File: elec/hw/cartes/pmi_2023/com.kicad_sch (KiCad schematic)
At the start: 37 parts, among them J7 USB4105-GF-A-060, Q2 2N7002, SW10 TS-1187A-B-A-B, SW7 MSS12C02LS-BB2.0, U32 ESP32-S3-WROOM-1

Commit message: small changes
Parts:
- SW10: footprint cocotter_others:TS-1187A-B-A-B -> cocotter_others:TSB001A3526A02; symbol cocotter_others:TS-1187A-B-A-B -> cocotter_others:TSB001A3526A02; JLCPCB C318884 -> C2888889
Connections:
- net EN_ESP32_3v3: now also SW10.2; no longer SW10.B (2)
- net GND_m: now also SW10.1; no longer SW10.A (1)
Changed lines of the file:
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@@
 	)
 	(symbol
-		(lib_id "cocotter_others:TS-1187A-B-A-B")
+		(lib_id "cocotter_others:TSB001A3526A02")
 		(at 69.85 148.59 90)
 		(unit 1)
@@
 			)
 		)
-		(property "Footprint" "cocotter_others:TS-1187A-B-A-B"
+		(property "Footprint" "cocotter_others:TSB001A3526A02"
 			(at 69.85 148.59 0)
 			(effects
@@
 			)
 		)
-		(property "Datasheet" ""
+		(property "Datasheet" "https://wmsc.lcsc.com/wmsc/upload/file/pdf/v2/lcsc/2108252230_BZCN-TSB001A3526A02_C2888889.pdf"
 			(at 74.93 148.59 0)
 			(effects
@@
 			)
 		)
-		(property "JLCPCB" "C318884"
+		(property "JLCPCB" "C2888889"
 			(at 74.93 149.86 0)
 			(effects
@@
 			)
 		)
-		(pin "A"
+		(pin "1"
 		)
-		(pin "B"
+		(pin "2"
 		)
 		(instances

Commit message: PAMI 2023: update jlc part number
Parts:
- R100, R82, R83, R91, R92, R97, R98, R99: JLCPCB C2991540 -> C21190
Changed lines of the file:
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@@
 			)
 		)
-		(property "JLCPCB" "C2991540"
+		(property "JLCPCB" "C21190"
 			(at 69.85 87.63 0)
 			(effects
@@
 			)
 		)
-		(property "JLCPCB" "C2991540"
+		(property "JLCPCB" "C21190"
 			(at 29.21 177.8 0)
 			(effects
@@
 			)
 		)
-		(property "JLCPCB" "C2991540"
+		(property "JLCPCB" "C21190"
 			(at 220.98 92.71 0)
 			(effects
@@
 			)
 		)
-		(property "JLCPCB" "C2991540"
+		(property "JLCPCB" "C21190"
 			(at 39.37 177.8 0)
 			(effects
@@
 			)
 		)
-		(property "JLCPCB" "C2991540"
+		(property "JLCPCB" "C21190"
 			(at 220.98 101.6 0)
 			(effects
@@
 			)
 		)
-		(property "JLCPCB" "C2991540"
+		(property "JLCPCB" "C21190"
 			(at 58.42 87.63 0)
 			(effects
@@
 			)
 		)
-		(property "JLCPCB" "C2991540"
+		(property "JLCPCB" "C21190"
 			(at 58.42 77.47 0)
 			(effects
@@
 			)
 		)
-		(property "JLCPCB" "C2991540"
+		(property "JLCPCB" "C21190"
 			(at 69.85 77.47 0)
 			(effects

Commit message: encoder resistors values corrected
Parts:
- SW10: value TS-1187A-B-A-B -> TSB001A3526A02
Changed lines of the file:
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@@
 			)
 		)
-		(property "Value" "TS-1187A-B-A-B"
+		(property "Value" "TSB001A3526A02"
 			(at 74.93 146.05 0)
 			(effects

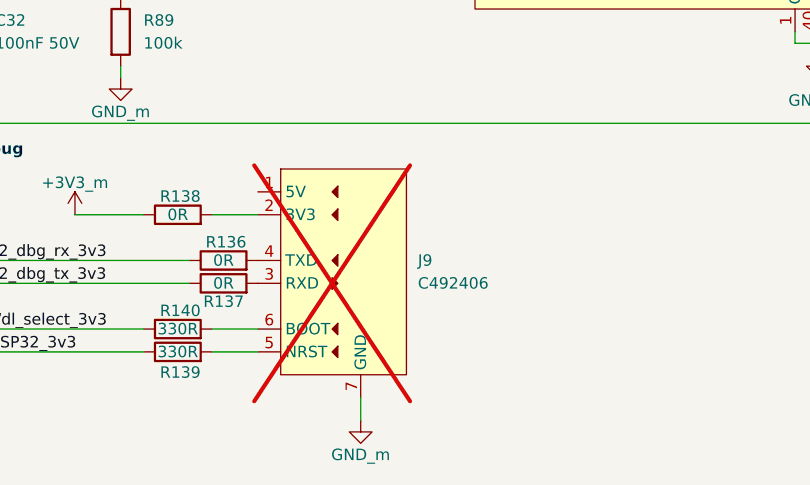
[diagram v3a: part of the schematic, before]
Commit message: XRA1200 replaced by TCA6408
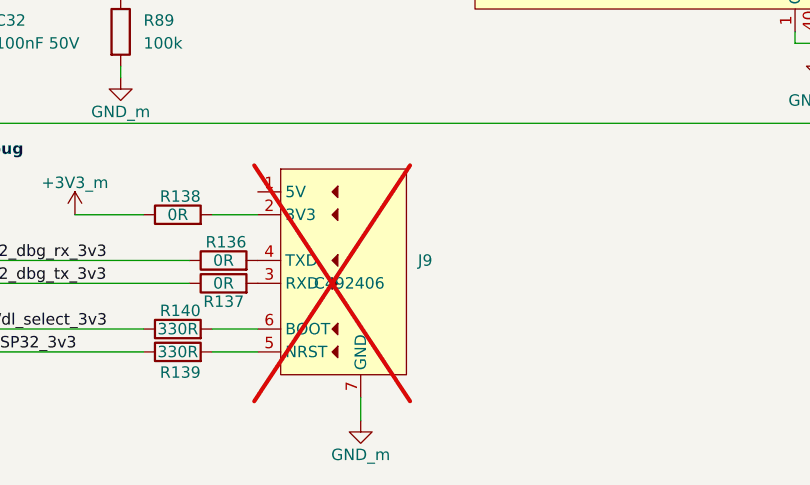
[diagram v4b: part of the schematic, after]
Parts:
- C32, C33, C34: JLCPCB C14663 -> (none); JLCPCB Part # (none) -> C14663
- C35: JLCPCB C15850 -> (none); JLCPCB Part # (none) -> C15850
- D4, D5: JLCPCB C2290 -> (none); JLCPCB Part # (none) -> C2290
- J7: JLCPCB C2927039 -> (none); JLCPCB Part # (none) -> C2927039
- J9: JLCPCB C492406 -> (none); JLCPCB Part # (none) -> C492406
- Q2: JLCPCB C8545 -> (none); JLCPCB Part # (none) -> C8545
- R100, R82, R83, R91, R92, R97, R98, R99: JLCPCB C21190 -> (none); JLCPCB Part # (none) -> C2991540
- R136, R137, R138: JLCPCB C431718 -> (none); JLCPCB Part # (none) -> C431718
- R139, R140: JLCPCB C23138 -> (none); JLCPCB Part # (none) -> C23138
- R84, R85, R86, R88, R89, R90, R93, R95, R96: JLCPCB C25803 -> (none); JLCPCB Part # (none) -> C25803
- R87: JLCPCB C23265 -> (none); JLCPCB Part # (none) -> C23265
- R94: JLCPCB C25804 -> (none); JLCPCB Part # (none) -> C25804
- SW10: JLCPCB C2888889 -> (none); JLCPCB Part # (none) -> C2888889
- SW7: JLCPCB C3008585 -> (none); JLCPCB Part # (none) -> C3008585
- U32: JLCPCB C2913204 -> (none); JLCPCB Part # (none) -> C2913204
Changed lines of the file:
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@@
 			)
 		)
-		(property "JLCPCB" "C25803"
+		(property "JLCPCB Part #" "C25803"
 			(at 97.79 130.81 0)
 			(effects
@@
 			)
 		)
-		(property "JLCPCB" "C15850"
+		(property "JLCPCB Part #" "C15850"
 			(at 208.28 33.02 0)
 			(effects
@@
 			)
 		)
-		(property "JLCPCB" "C23138"
+		(property "JLCPCB Part #" "C23138"
 			(at 104.14 181.61 0)
 			(effects
@@
 			)
 		)
-		(property "JLCPCB" "C2888889"
+		(property "JLCPCB Part #" "C2888889"
 			(at 74.93 149.86 0)
 			(effects
@@
 			)
 		)
-		(property "JLCPCB" "C8545"
+		(property "JLCPCB Part #" "C8545"
 			(at 234.95 144.78 0)
 			(effects
@@
 			)
 		)
-		(property "JLCPCB" "C14663"
+		(property "JLCPCB Part #" "C14663"
 			(at 186.69 33.02 0)
 			(effects
@@
 			)
 		)
-		(property "JLCPCB" "C25803"
+		(property "JLCPCB Part #" "C25803"
 			(at 85.09 63.5 0)
 			(effects
@@
 			)
 		)
-		(property "JLCPCB" "C2290"
+		(property "JLCPCB Part #" "C2290"
 			(at 29.21 185.42 0)
 			(effects
@@
 			)
 		)
-		(property "JLCPCB" "C25804"
+		(property "JLCPCB Part #" "C25804"
 			(at 229.87 125.73 0)
 			(effects
@@
 			)
 		)
-		(property "JLCPCB" "C25803"
+		(property "JLCPCB Part #" "C25803"
 			(at 82.55 130.81 0)
 			(effects
@@
 			)
 		)
-		(property "JLCPCB" "C23138"
+		(property "JLCPCB Part #" "C23138"
 			(at 104.14 184.15 0)
 			(effects
@@
 			)
 		)
-		(property "JLCPCB" "C14663"
+		(property "JLCPCB Part #" "C14663"
 			(at 93.98 60.96 0)
 			(effects
@@
 			)
 		)
-		(property "JLCPCB" "C14663"
+		(property "JLCPCB Part #" "C14663"
 			(at 80.01 148.59 0)
 			(effects
@@
 			)
 		)
-		(property "JLCPCB" "C431718"
+		(property "JLCPCB Part #" "C431718"
 			(at 109.22 176.53 0)
 			(effects
@@
 			)
 		)
-		(property "JLCPCB" "C2290"
+		(property "JLCPCB Part #" "C2290"
 			(at 39.37 185.42 0)
 			(effects
@@
 			)
 		)
-		(property "JLCPCB" "C21190"
+		(property "JLCPCB Part #" "C2991540"
 			(at 69.85 87.63 0)
 			(effects
@@
 			)
 		)
-		(property "JLCPCB" "C3008585"
+		(property "JLCPCB Part #" "C3008585"
 			(at 227.33 133.35 0)
 			(effects
@@
 			)
 		)
-		(property "JLCPCB" "C21190"
+		(property "JLCPCB Part #" "C2991540"
 			(at 29.21 177.8 0)
 			(effects
@@
 			)
 		)
-		(property "JLCPCB" "C21190"
+		(property "JLCPCB Part #" "C2991540"
 			(at 220.98 92.71 0)
 			(effects
@@
 			)
 		)
-		(property "JLCPCB" "C25803"
+		(property "JLCPCB Part #" "C25803"
 			(at 243.84 146.05 0)
 			(effects
@@
 			)
 		)
-		(property "JLCPCB" "C23265"
+		(property "JLCPCB Part #" "C23265"
 			(at 93.98 50.8 0)
 			(effects
@@
 			)
 		)
-		(property "JLCPCB" "C21190"
+		(property "JLCPCB Part #" "C2991540"
 			(at 39.37 177.8 0)
 			(effects
@@
 			)
 		)
-		(property "JLCPCB" "C25803"
+		(property "JLCPCB Part #" "C25803"
 			(at 85.09 50.8 0)
 			(effects
@@
 			)
 		)
-		(property "JLCPCB" "C431718"
+		(property "JLCPCB Part #" "C431718"
 			(at 104.14 168.91 0)
 			(effects
@@
 			)
 		)
-		(property "JLCPCB" "C21190"
+		(property "JLCPCB Part #" "C2991540"
 			(at 220.98 101.6 0)
 			(effects
@@
 			)
 		)
-		(property "JLCPCB" "C492406"
-			(at 130.81 176.5299 0)
+		(property "JLCPCB Part #" "C492406"
+			(at 123.19 176.53 0)
 			(effects
 				(font
 					(size 1.27 1.27)
 				)
-				(justify left)
 			)
 		)
@@
 			)
 		)
-		(property "JLCPCB" "C25803"
+		(property "JLCPCB Part #" "C25803"
 			(at 217.17 135.89 0)
 			(effects
@@
 			)
 		)
-		(property "JLCPCB" "C2927039"
+		(property "JLCPCB Part #" "C2927039"
 			(at 273.05 109.22 0)
 			(effects
@@
 			)
 		)
-		(property "JLCPCB" "C21190"
+		(property "JLCPCB Part #" "C2991540"
 			(at 58.42 87.63 0)
 			(effects
@@
 			)
 		)
-		(property "JLCPCB" "C21190"
+		(property "JLCPCB Part #" "C2991540"
 			(at 58.42 77.47 0)
 			(effects
@@
 			)
 		)
-		(property "JLCPCB" "C431718"
+		(property "JLCPCB Part #" "C431718"
 			(at 109.22 173.99 0)
 			(effects
@@
 			)
 		)
-		(property "JLCPCB" "C25803"
+		(property "JLCPCB Part #" "C25803"
 			(at 229.87 92.71 0)
 			(effects
@@
 			)
 		)
-		(property "JLCPCB" "C25803"
+		(property "JLCPCB Part #" "C25803"
 			(at 238.76 92.71 0)
 			(effects
@@
 			)
 		)
-		(property "JLCPCB" "C21190"
+		(property "JLCPCB Part #" "C2991540"
 			(at 69.85 77.47 0)
 			(effects
@@
 			)
 		)
-		(property "JLCPCB" "C2913204"
+		(property "JLCPCB Part #" "C2913204"
 			(at 175.26 96.52 0)
 			(effects
@@
 			)
 		)
-		(property "JLCPCB" "C25803"
+		(property "JLCPCB Part #" "C25803"
 			(at 97.79 148.59 0)
 			(effects

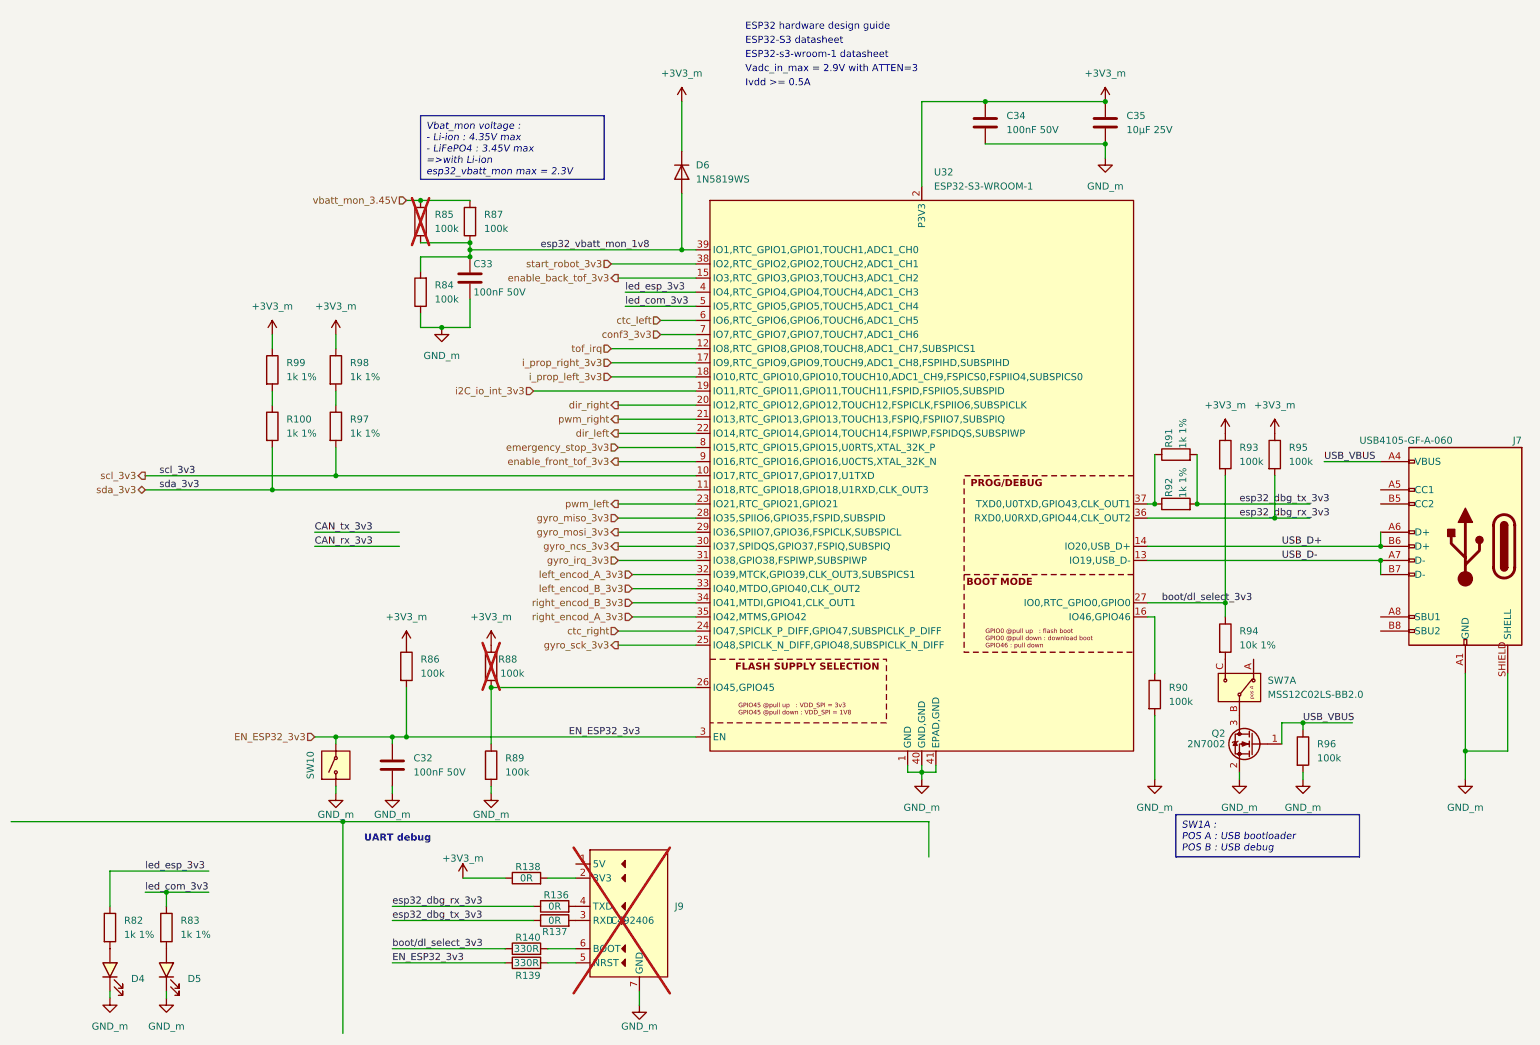
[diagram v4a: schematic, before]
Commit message: bom updated and component selection optimized to decrease bom cost
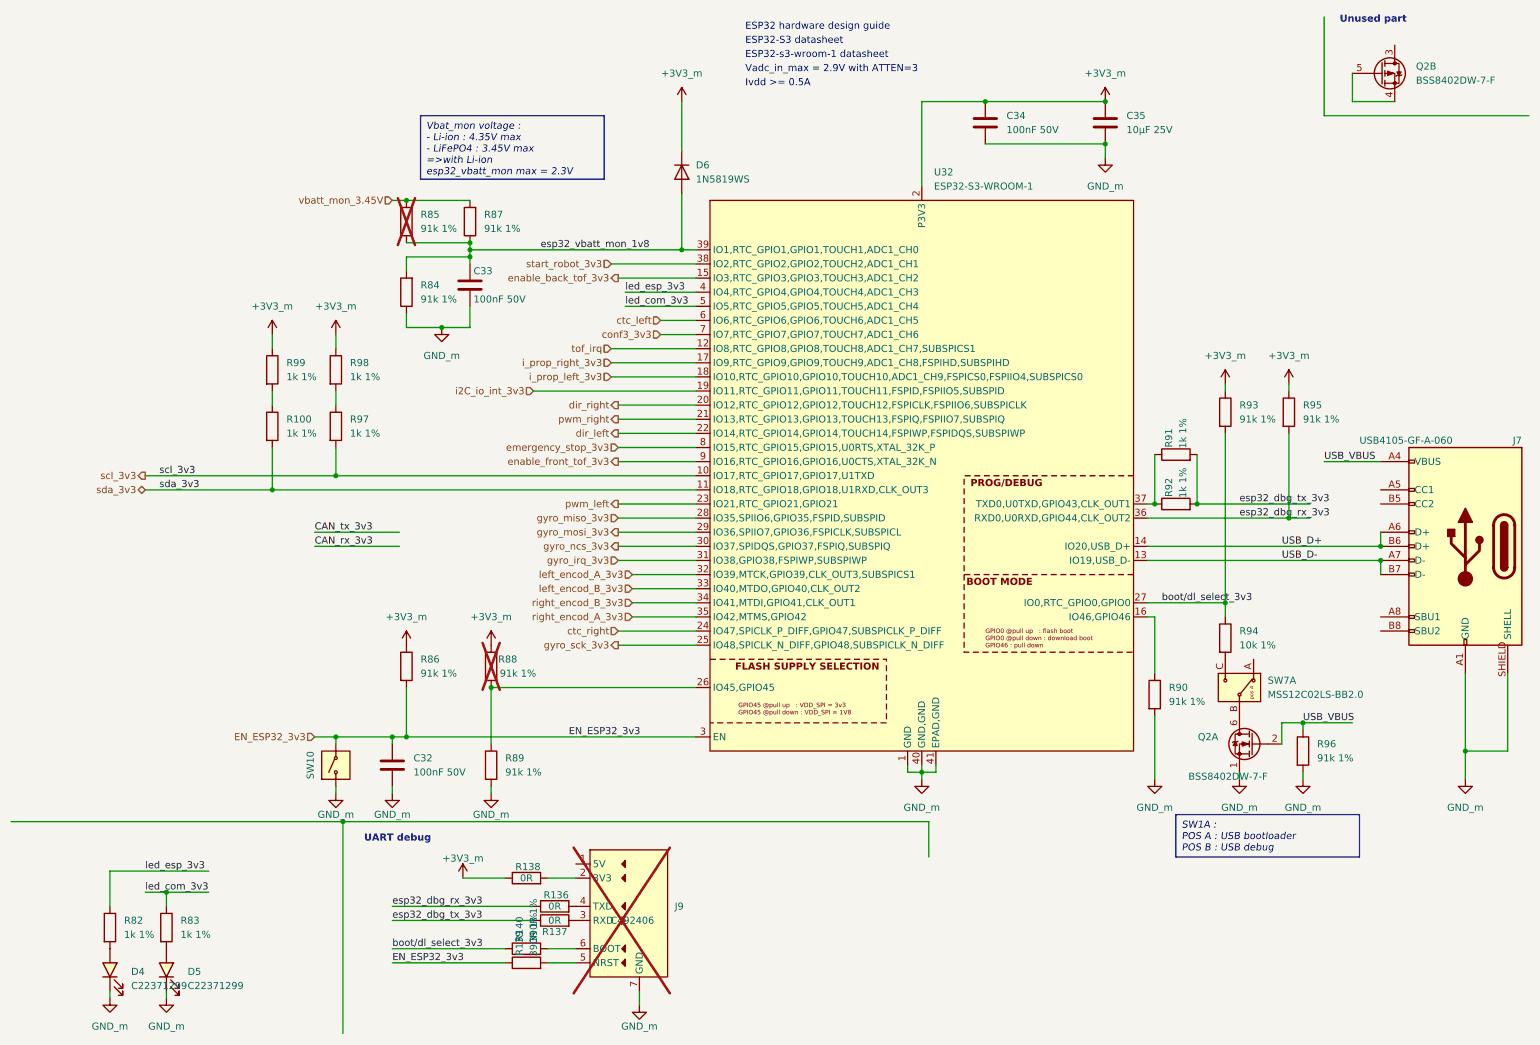
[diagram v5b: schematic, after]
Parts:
- removed Q2: 2N7002, Package_TO_SOT_SMD:SOT-23, symbol cocotter_transistors:2N7002
- added Q2: BSS8402DW-7-F, cocotter_transistors:SOT-363_SC-70-6, symbol cocotter_transistors:BSS8402DW-7-F
- D4, D5: value white, 0603 -> green, 0603; symbol cocotter_diodes:white_led_0603 -> cocotter_diodes:green_led_0603; DIGIKEY_REF (none) -> 3147-B19Y1UYG-20C000313U1930CT-ND; JLCPCB Part # C2290 -> C22371299; MOUSER_REF (none) -> 710-150060VS55040
- R139, R140: value 330R -> 390R 1%; symbol cocotter_resistors:R_330R_0603_1% -> cocotter_resistors:R_390R_0603_1%; JLCPCB Part # C23138 -> C23151; Specification 330R 0603 1% 100mW -> 390R 0603 1% 100mW
- R84, R85, R86, R88, R89, R90, R93, R95, R96: value 100k -> 91k 1%; symbol cocotter_resistors:R_100k_0603_1% -> cocotter_resistors:R_91k_0603_1%; JLCPCB Part # C25803 -> C23265; Specification 100k 0603 1% 100mW -> 91k 0603 1% 100mW; mouser 603-RC0603FR-10100KL -> (none)
- R87: value 100k -> 91k 1%
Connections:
- net GND_m: now also Q2.1 (SN)
- net USB_VBUS: now also Q2.2 (GN)
- net at SW7.B: now also Q2.6 (DN)
- new net: Q2.4 (SP), Q2.5 (GP)
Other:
- note added: "Unused part"
- moved on the sheet: C33, R84, R85, R93, R95

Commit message: second round of review corrections
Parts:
- removed Q2: BSS8402DW-7-F, cocotter_transistors:SOT-363_SC-70-6, symbol cocotter_transistors:BSS8402DW-7-F
- added Q4: SI2310, cocotter_transistors:SOT-23-3, symbol cocotter_transistors:SI2310
- added TP18, TP19: TestPoint, cocotter_others:testpoint-THT-0.5mm, symbol cocotter_others:TestPoint
- U32: symbol cocotter_ic:ESP32-S3-WROOM-1-N8R2 -> cocotter_ic:ESP32-S3-WROOM-1U-N8R2; JLCPCB Part # C2913204 -> C3013944
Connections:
- net GND_m: now also SW7.MP, Q4.2 (S)
- net USB_VBUS: now also Q4.1 (G)
- net scl_3v3: now also TP18.1
- net sda_3v3: now also TP19.1
- net at SW7.B: now also Q4.3 (D)
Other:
- note removed: "Unused part"

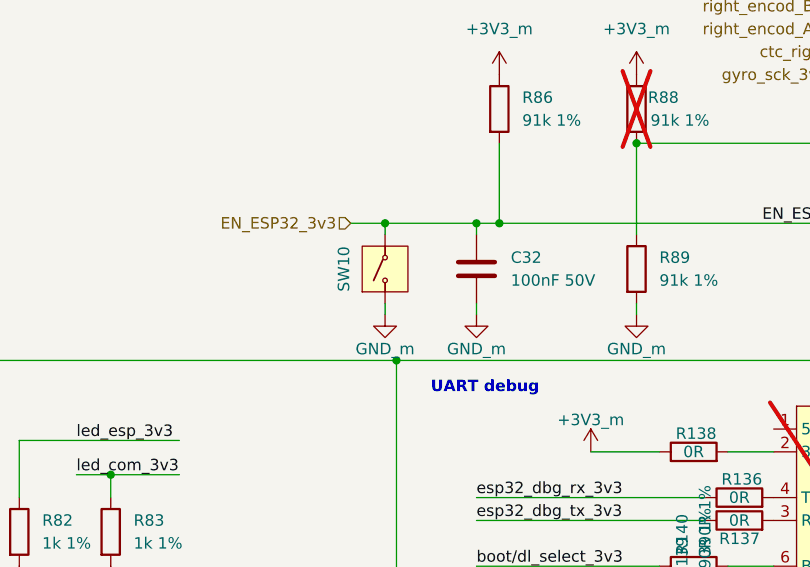
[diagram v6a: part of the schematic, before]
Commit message: review number 3 taken into account
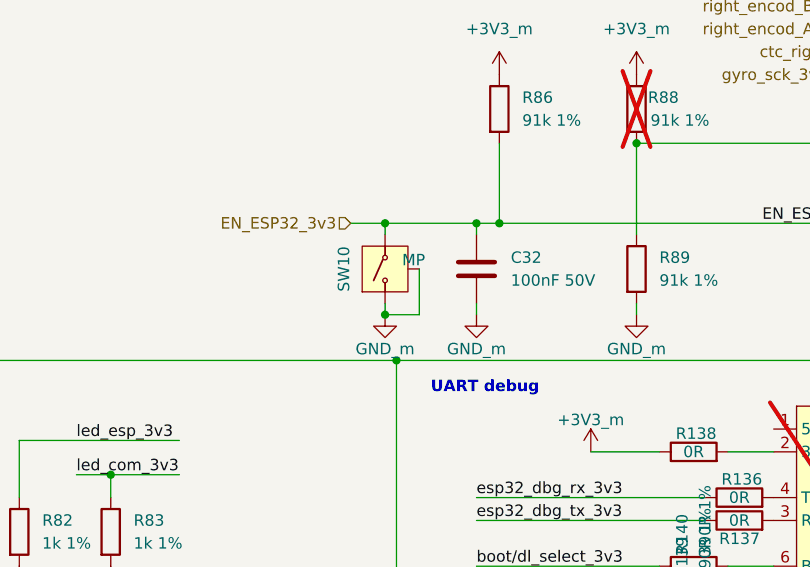
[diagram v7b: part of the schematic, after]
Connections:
- net GND_m: now also SW10.MP
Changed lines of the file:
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@@
+	)
+	(junction
+		(at 69.85 153.67)
+		(diameter 0)
+		(color 0 0 0 0)
 	)
 	(junction
@@
 	(wire
 		(pts
+			(xy 73.66 148.59) (xy 73.66 153.67)
+		)
+		(stroke
+			(width 0)
+			(type default)
+		)
+	)
+	(wire
+		(pts
 			(xy 107.95 184.15) (xy 113.03 184.15)
 		)
@@
 		(pts
 			(xy 119.38 58.42) (xy 134.62 58.42)
+		)
+		(stroke
+			(width 0)
+			(type default)
+		)
+	)
+	(wire
+		(pts
+			(xy 69.85 153.67) (xy 73.66 153.67)
 		)
 		(stroke
@@
 		(pin "2"
 		)
+		(pin "MP"
+		)
 		(instances

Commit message: pmi board V2, ready for review
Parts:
- added R149, R55, R59, R61: 1k 1%, cocotter_resistor:r0603_reflow, symbol cocotter_resistors:R_1k_0603_1%
- added R80: 0R, cocotter_resistor:r0603_reflow, symbol cocotter_resistors:R_0R_0603
- Q4, R94, R96, SW7: now not fitted
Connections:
- net i_prop_left_3v3 is gone; now on net scl_3v3: U32.18 (IO10,RTC_GPIO10,GPIO10,TOUCH10,ADC1_CH9,FSPICS0,FSPIIO4,SUBSPICS0)
- net i_prop_right_3v3 is gone; now on net sda_3v3: U32.17 (IO9,RTC_GPIO9,GPIO9,TOUCH9,ADC1_CH8,FSPIHD,SUBSPIHD)
- net +3V3_m: now also R55.1, R61.1
- net GND_m: now also R80.2; no longer SW7.MP
- net boot/dl_select_3v3: now also R80.1
- net scl_3v3: now also R59.2; no longer R97.2, TP18.1, U32.10 (IO17,RTC_GPIO17,GPIO17,U1TXD)
- net sda_3v3: now also R149.2; no longer R100.2, TP19.1, U32.11 (IO18,RTC_GPIO18,GPIO18,U1RXD,CLK_OUT3)
- new net: R55.2, R59.1
- new net: R149.1, R61.2
- new net scl_tof_3v3: R100.2, TP19.1, U32.11 (IO18,RTC_GPIO18,GPIO18,U1RXD,CLK_OUT3)
- new net sda_tof_3v3: R97.2, TP18.1, U32.10 (IO17,RTC_GPIO17,GPIO17,U1TXD)
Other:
- moved on the sheet: J9, R100, R136, R137, R138, R139, R140, R97, R98, R99
